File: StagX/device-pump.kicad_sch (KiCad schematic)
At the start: 1 part

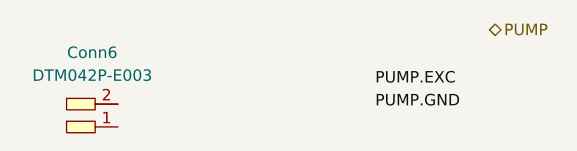
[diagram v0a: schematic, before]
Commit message: Completed shutdown loop
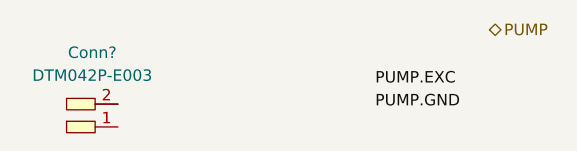
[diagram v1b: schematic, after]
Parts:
- renumbered Conn6 to Conn?
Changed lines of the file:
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@@
   (symbol (lib_id "Connectors_SUFST:Deutsch_DTM_2P_Pin") (at 132.08 80.01 0) (unit 1)
     (in_bom yes) (on_board yes) (dnp no) (fields_autoplaced)
-    (property "Reference" "Conn6" (at 131.1275 78.74 0)
+    (property "Reference" "Conn?" (at 131.1275 78.74 0)
       (effects (font (size 1.27 1.27)))
     )
@@
       (project "StagX"
         (path "/03011643-0690-4b85-ab78-d6a62dae52b1/51825ed1-c28d-47fe-be22-df39d19065ff"
-          (reference "Conn6") (unit 1)
+          (reference "Conn?") (unit 1)
         )
         (path "/03011643-0690-4b85-ab78-d6a62dae52b1/2cf8afa7-2cb2-4c65-9a6a-3a43fa257b78"
-          (reference "Conn7") (unit 1)
+          (reference "Conn?") (unit 1)
         )
       )
